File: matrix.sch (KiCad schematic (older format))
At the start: 136 parts, among them SW1 KEYSW, SW10 KEYSW, SW11 KEYSW, SW12 KEYSW, SW13 KEYSW, SW14 KEYSW, SW15 KEYSW, SW16 KEYSW, SW17 KEYSW, SW18 KEYSW, SW19 KEYSW, SW2 KEYSW, SW20 KEYSW, SW21 KEYSW, SW22 KEYSW, SW23 KEYSW, SW24 KEYSW, SW25 KEYSW, SW26 KEYSW, SW27 KEYSW, SW28 KEYSW, SW29 KEYSW, SW3 KEYSW, SW30 KEYSW, SW31 KEYSW, SW32 KEYSW, SW33 KEYSW, SW34 KEYSW, SW35 KEYSW, SW36 KEYSW, SW37 KEYSW, SW38 KEYSW, SW39 KEYSW, SW4 KEYSW, SW40 KEYSW, SW41 KEYSW, SW42 KEYSW, SW43 KEYSW, SW44 KEYSW, SW45 KEYSW, SW46 KEYSW, SW47 KEYSW, SW48 KEYSW, SW49 KEYSW, SW5 KEYSW, SW50 KEYSW, SW51 KEYSW, SW52 KEYSW, SW53 KEYSW, SW54 KEYSW, SW55 KEYSW, SW56 KEYSW, SW57 KEYSW, SW58 KEYSW, SW59 KEYSW, SW6 KEYSW, SW60 KEYSW, SW61 KEYSW, SW62 KEYSW, SW63 KEYSW, SW64 KEYSW, SW65 KEYSW, SW66 KEYSW, SW67 KEYSW, SW68 KEYSW, SW7 KEYSW, SW8 KEYSW, SW9 KEYSW

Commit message: Misc cleanup, delete tracks to prepare for bigger changes
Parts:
- SW1, SW10, SW11, SW12, SW13, SW15, SW17, SW18, SW19, SW2, SW20, SW21, SW22, SW23, SW24, SW25, SW26, SW27, SW28, SW3, SW30, SW32, SW33, SW34, SW35, SW36, SW37, SW38, SW39, SW4, SW40, SW41, SW42, SW44, SW46, SW47, SW48, SW49, SW5, SW50, SW51, SW52, SW53, SW54, SW55, SW57, SW58, SW6, SW65, SW66, SW67, SW68, SW7, SW8, SW9: footprint (none) -> MX_Alps_Hybrid:MX-1U
- SW14: footprint (none) -> MX_Alps_Hybrid:MX-2U
- SW16, SW29: footprint (none) -> MX_Alps_Hybrid:MX-1.5U
- SW31, SW56: footprint (none) -> MX_Alps_Hybrid:MX-1.75U
- SW43, SW45: footprint (none) -> MX_Alps_Hybrid:MX-2.25U
- SW59, SW60, SW61: footprint (none) -> MX_Alps_Hybrid:MX-1.25U

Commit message: Move diodes to key area
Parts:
- D1, D10, D11, D12, D13, D14, D15, D16, D17, D18, D19, D2, D20, D21, D22, D23, D24, D25, D26, D27, D28, D29, D3, D30, D31, D32, D33, D34, D35, D36, D37, D38, D39, D4, D40, D41, D42, D43, D44, D45, D46, D47, D48, D49, D5, D50, D51, D52, D53, D54, D55, D56, D57, D58, D59, D6, D60, D61, D62, D63, D64, D65, D66, D67, D68, D7, D8, D9: footprint cftkb:D_DO-35_SOD27_P5.08mm_Horizontal -> keyboard_parts:D_SOD123_axial

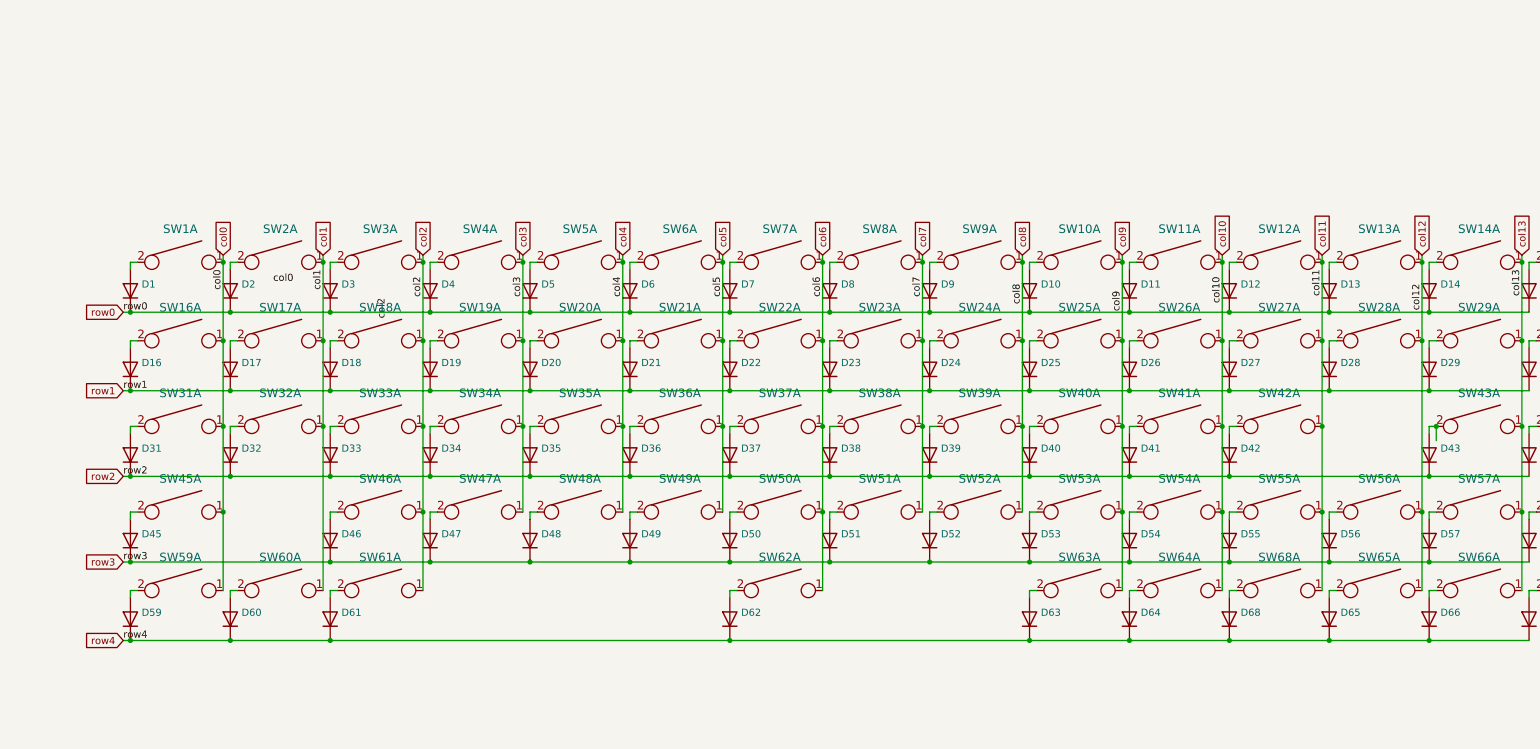
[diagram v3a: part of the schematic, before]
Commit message: Add rotary encoder
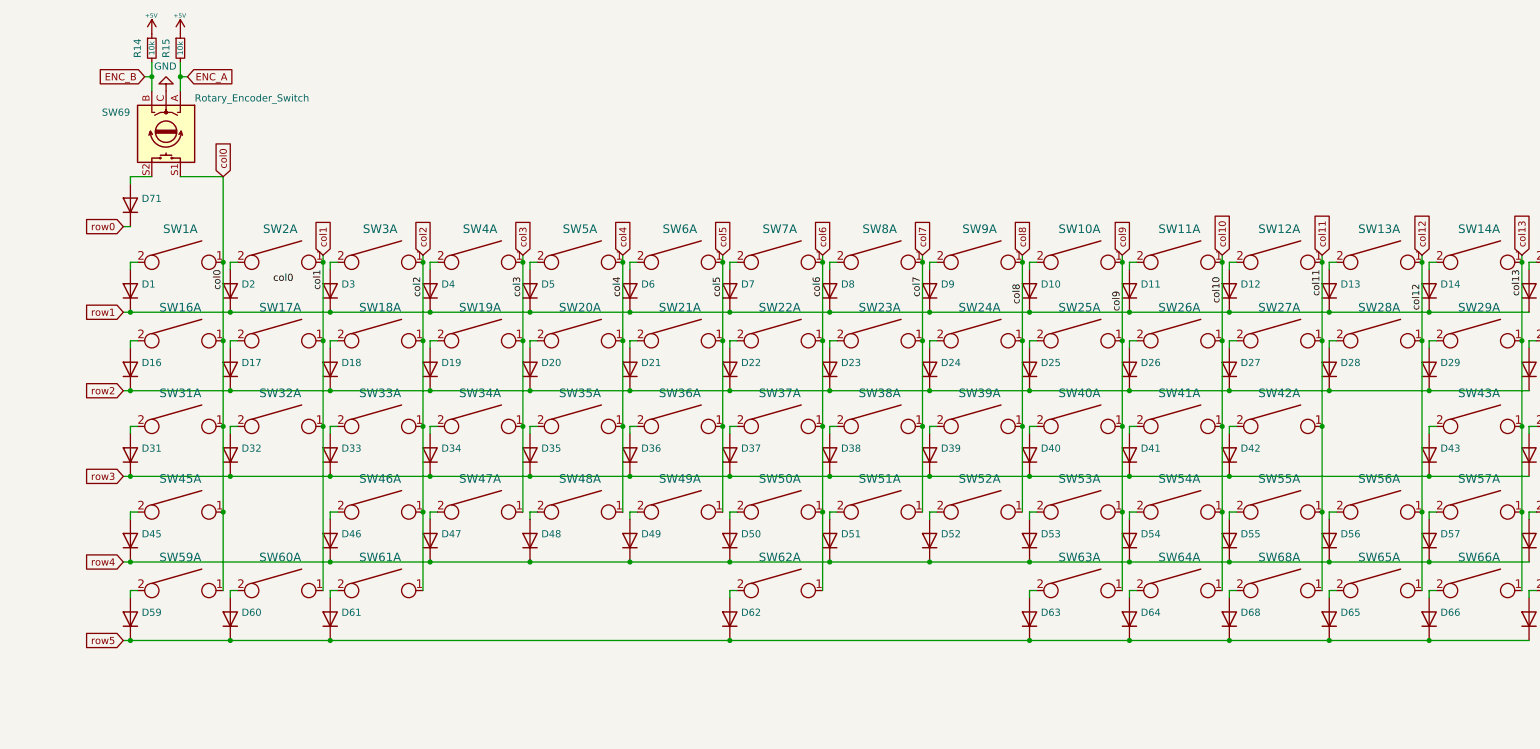
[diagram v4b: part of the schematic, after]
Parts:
- added D71: (no value), keyboard_parts:D_SOD123_axial, symbol Device:D
- added R14, R15: 10k, cftkb:R_Axial_DIN0204_L3.6mm_D1.6mm_P5.08mm_Horizontal, symbol Device:R_Small
- added SW69: Rotary_Encoder_Switch, Gigahawk:482016514001, symbol Device:Rotary_Encoder_Switch
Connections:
- net col0: now also SW69.S1
- net row0: now also D71.1 (K); no longer D1.1 (K), D10.1 (K), D11.1 (K), D12.1 (K), D13.1 (K), D14.1 (K), D15.1 (K), D2.1 (K), D3.1 (K), D4.1 (K), D5.1 (K), D6.1 (K), D7.1 (K), D8.1 (K), D9.1 (K)
- net row1: now also D1.1 (K), D10.1 (K), D11.1 (K), D12.1 (K), D13.1 (K), D14.1 (K), D15.1 (K), D2.1 (K), D3.1 (K), D4.1 (K), D5.1 (K), D6.1 (K), D7.1 (K), D8.1 (K), D9.1 (K); no longer D16.1 (K), D17.1 (K), D18.1 (K), D19.1 (K), D20.1 (K), D21.1 (K), D22.1 (K), D23.1 (K), D24.1 (K), D25.1 (K), D26.1 (K), D27.1 (K), D28.1 (K), D29.1 (K), D30.1 (K)
- net row2: now also D16.1 (K), D17.1 (K), D18.1 (K), D19.1 (K), D20.1 (K), D21.1 (K), D22.1 (K), D23.1 (K), D24.1 (K), D25.1 (K), D26.1 (K), D27.1 (K), D28.1 (K), D29.1 (K), D30.1 (K); no longer D31.1 (K), D32.1 (K), D33.1 (K), D34.1 (K), D35.1 (K), D36.1 (K), D37.1 (K), D38.1 (K), D39.1 (K), D40.1 (K), D41.1 (K), D42.1 (K), D43.1 (K), D44.1 (K)
- net row3: now also D31.1 (K), D32.1 (K), D33.1 (K), D34.1 (K), D35.1 (K), D36.1 (K), D37.1 (K), D38.1 (K), D39.1 (K), D40.1 (K), D41.1 (K), D42.1 (K), D43.1 (K), D44.1 (K); no longer D45.1 (K), D46.1 (K), D47.1 (K), D48.1 (K), D49.1 (K), D50.1 (K), D51.1 (K), D52.1 (K), D53.1 (K), D54.1 (K), D55.1 (K), D56.1 (K), D57.1 (K), D58.1 (K)
- net row4: now also D45.1 (K), D46.1 (K), D47.1 (K), D48.1 (K), D49.1 (K), D50.1 (K), D51.1 (K), D52.1 (K), D53.1 (K), D54.1 (K), D55.1 (K), D56.1 (K), D57.1 (K), D58.1 (K); no longer D59.1 (K), D60.1 (K), D61.1 (K), D62.1 (K), D63.1 (K), D64.1 (K), D65.1 (K), D66.1 (K), D67.1 (K), D68.1 (K)
- new net: D71.2 (A), SW69.S2
- new net +5V: R14.1, R15.1
- new net ENC_A: R15.2, SW69.A
- new net ENC_B: R14.2, SW69.B
- new net GND: SW69.C
- new net row5: D59.1 (K), D60.1 (K), D61.1 (K), D62.1 (K), D63.1 (K), D64.1 (K), D65.1 (K), D66.1 (K), D67.1 (K), D68.1 (K)
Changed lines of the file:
@@
 Wire Wire Line
 	12000 3850 12700 3850
-Text Label 2850 3300 0    50   ~ 0
-row0
-Text Label 2850 3850 0    50   ~ 0
-row1
 Wire Wire Line
 	2900 4450 3600 4450
@@
 	2850 4450 2900 4450
 Connection ~ 2900 4450
-Text Label 2850 4450 0    50   ~ 0
-row2
 Wire Wire Line
 	2850 5050 2900 5050
 Connection ~ 2900 5050
-Text Label 2850 5050 0    50   ~ 0
-row3
 Wire Wire Line
 	2850 5600 2900 5600
@@
 Wire Wire Line
 	2900 5600 3600 5600
-Text Label 2850 5600 0    50   ~ 0
-row4
 Text Label 3900 3100 0    50   ~ 0
 col0
@@
 Text Label 3550 3000 3    50   ~ 0
 col0
-Text Label 4700 3200 3    50   ~ 0
-col2
 Text Label 4950 3050 3    50   ~ 0
 col2
@@
 Text Label 13350 3050 3    50   ~ 0
 col14
+Text GLabel 2850 2700 0    50   Input ~ 0
+row0
 Text GLabel 2850 3300 0    50   Input ~ 0
-row0
+row1
 Text GLabel 2850 3850 0    50   Input ~ 0
-row1
+row2
 Text GLabel 2850 4450 0    50   Input ~ 0
-row2
+row3
 Text GLabel 2850 5050 0    50   Input ~ 0
-row3
-Text GLabel 2850 5600 0    50   Input ~ 0
 row4
-Text GLabel 3550 2900 1    50   Input ~ 0
+Text GLabel 3550 2350 1    50   Input ~ 0
 col0
 Text GLabel 4250 2900 1    50   Input ~ 0
@@
 Text Notes 15550 11050 2    50   ~ 0
 1.1
-Wire Wire Line
-	3550 2900 3550 2950
 Connection ~ 3550 2950
 Wire Wire Line
@@
 Wire Wire Line
 	13350 4700 13350 5250
-Wire Wire Line
-	12050 4200 12050 4100
-Connection ~ 12050 4100
 $Comp
 L keyboard_parts:KEYSW SW1
@@
 Wire Wire Line
 	3100 8400 3100 9700
+$Comp
+L Device:Rotary_Encoder_Switch SW69
+U 1 1 5F364C90
+P 3150 2050
+F 0 "SW69" V 3000 1600 50  0000 L CNN
+F 1 "Rotary_Encoder_Switch" V 2900 2250 50  0000 L CNN
+F 2 "Gigahawk:482016514001" H 3000 2210 50  0001 C CNN
+F 3 "~" H 3150 2310 50  0001 C CNN
+	1    3150 2050
+	0    1    1    0
+$EndComp
+$Comp
+L power:GND #PWR?
+U 1 1 5F418DFD
+P 3150 1750
+AR Path="/5F418DFD" Ref="#PWR?"  Part="1"
+AR Path="/5F37C842/5F418DFD" Ref="#PWR0104"  Part="1"
+F 0 "#PWR0104" H 3150 1500 50  0001 C CNN
+F 1 "GND" H 3155 1577 50  0000 C CNN
+F 2 "" H 3150 1750 50  0001 C CNN
+F 3 "" H 3150 1750 50  0001 C CNN
+	1    3150 1750
+	-1   0    0    1
+$EndComp
+Text GLabel 3300 1650 2    50   Input ~ 0
+ENC_A
+Text GLabel 3000 1650 0    50   Input ~ 0
+ENC_B
+Wire Wire Line
+	3250 1750 3250 1650
+Wire Wire Line
+	3250 1650 3300 1650
+Wire Wire Line
+	3050 1750 3050 1650
+Wire Wire Line
+	3050 1650 3000 1650
+$Comp
+L Device:D D71
+U 1 1 5F5DE18A
+P 2900 2550
+F 0 "D71" V 2946 2471 50  0000 R CNN
+F 1 " " V 2855 2471 50  0000 R CNN
+F 2 "keyboard_parts:D_SOD123_axial" H 2900 2550 50  0001 C CNN
+F 3 "~" H 2900 2550 50  0001 C CNN
+	1    2900 2550
+	0    -1   -1   0
+$EndComp
+Wire Wire Line
+	2900 2400 2900 2350
+Wire Wire Line
+	2900 2350 3050 2350
+Text GLabel 2850 5600 0    50   Input ~ 0
+row5
+Wire Wire Line
+	3250 2350 3550 2350
+Wire Wire Line
+	3550 2350 3550 2950
+Wire Wire Line
+	2900 2700 2850 2700
+$Comp
+L Device:R_Small R?
+U 1 1 5FA0E8A0
+P 3250 1450
+AR Path="/5FA0E8A0" Ref="R?"  Part="1"
+AR Path="/5F37C842/5FA0E8A0" Ref="R15"  Part="1"
+F 0 "R15" V 3150 1450 50  0000 C CNN
+F 1 "10k" V 3250 1450 39  0000 C CNN
+F 2 "cftkb:R_Axial_DIN0204_L3.6mm_D1.6mm_P5.08mm_Horizontal" H 3250 1450 50  0001 C CNN
+F 3 "~" H 3250 1450 50  0001 C CNN
+	1    3250 1450
+	1    0    0    -1
+$EndComp
+$Comp
+L Device:R_Small R?
+U 1 1 5FA0E8A6
+P 3050 1450
+AR Path="/5FA0E8A6" Ref="R?"  Part="1"
+AR Path="/5F37C842/5FA0E8A6" Ref="R14"  Part="1"
+F 0 "R14" V 2950 1450 50  0000 C CNN
+F 1 "10k" V 3050 1450 39  0000 C CNN
+F 2 "cftkb:R_Axial_DIN0204_L3.6mm_D1.6mm_P5.08mm_Horizontal" H 3050 1450 50  0001 C CNN
+F 3 "~" H 3050 1450 50  0001 C CNN
+	1    3050 1450
+	1    0    0    -1
+$EndComp
+$Comp
+L power:+5V #PWR?
+U 1 1 5FA6C502
+P 3050 1350
+AR Path="/5FA6C502" Ref="#PWR?"  Part="1"
+AR Path="/5F37C842/5FA6C502" Ref="#PWR0117"  Part="1"
+F 0 "#PWR0117" H 3050 1440 20  0001 C CNN
+F 1 "+5V" H 3046 1478 30  0000 C CNN
+F 2 "" H 3050 1350 60  0000 C CNN
+F 3 "" H 3050 1350 60  0000 C CNN
+	1    3050 1350
+	1    0    0    -1
+$EndComp
+Connection ~ 3050 1650
+$Comp
+L power:+5V #PWR?
+U 1 1 5FBD86D1
+P 3250 1350
+AR Path="/5FBD86D1" Ref="#PWR?"  Part="1"
+AR Path="/5F37C842/5FBD86D1" Ref="#PWR0120"  Part="1"
+F 0 "#PWR0120" H 3250 1440 20  0001 C CNN
+F 1 "+5V" H 3246 1478 30  0000 C CNN
+F 2 "" H 3250 1350 60  0000 C CNN
+F 3 "" H 3250 1350 60  0000 C CNN
+	1    3250 1350
+	1    0    0    -1
+$EndComp
+Wire Wire Line
+	3050 1550 3050 1650
+Wire Wire Line
+	3250 1550 3250 1650
+Connection ~ 3250 1650
 $EndSCHEMATC
